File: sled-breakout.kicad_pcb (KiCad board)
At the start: 2 copper layers, 38 x 46 mm, 11 parts, among them J1 Conn_01x09, J2 Conn_01x09, J3 Conn_01x07, U1 sled1735

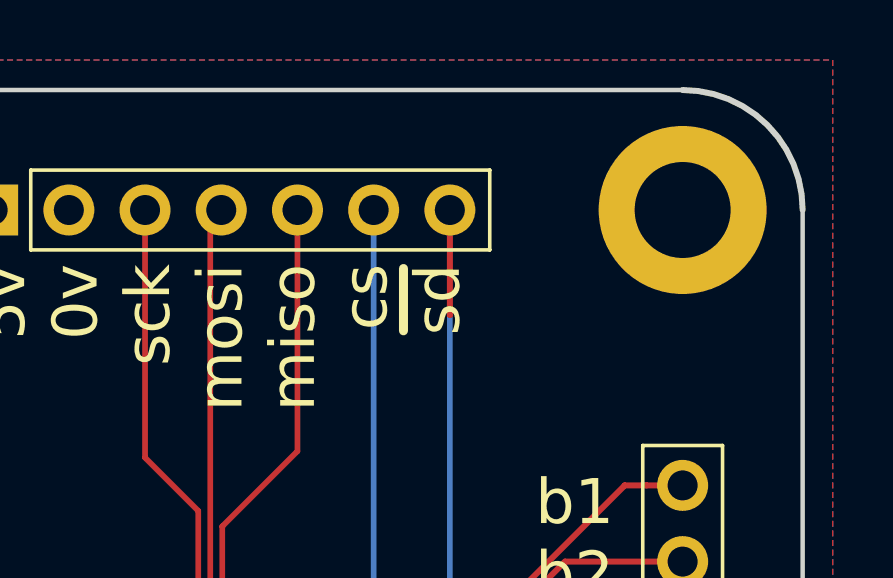
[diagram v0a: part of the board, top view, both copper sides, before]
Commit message: removed old trace
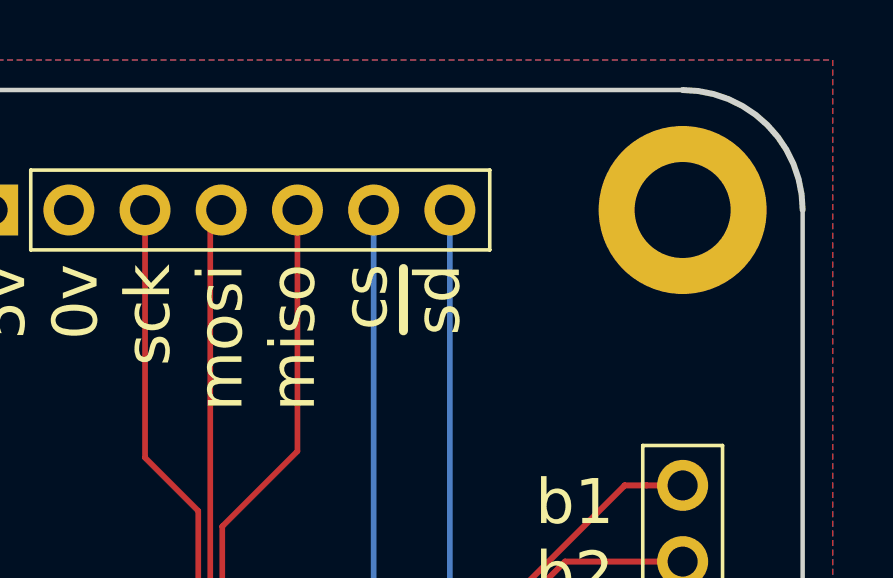
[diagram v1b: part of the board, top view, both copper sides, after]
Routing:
- net SHUTDOWN: track 39.5 -> 36.0 mm
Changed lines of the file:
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@@
     (thickness 1.6)
     (drawings 21)
-    (tracks 118)
+    (tracks 116)
     (zones 0)
     (modules 11)
@@
   (segment (start 188.453576 114.953576) (end 188.55 115.05) (width 0.19) (layer F.Cu) (net 25))
   (via (at 188.55 115.05) (size 0.8) (drill 0.4) (layers F.Cu B.Cu) (net 25))
-  (segment (start 195.24 91) (end 195.24 94.49) (width 0.2) (layer F.Cu) (net 25))
-  (segment (start 195.24 94.49) (end 195.25 94.5) (width 0.2) (layer F.Cu) (net 25))
   (zone (net 1) (net_name Earth) (layer F.Cu) (hatch edge 0.508)
     (connect_pads (clearance 0.508))
